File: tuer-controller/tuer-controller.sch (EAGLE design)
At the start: 19 parts, among them IC1 ATTINY24/44/84-PU

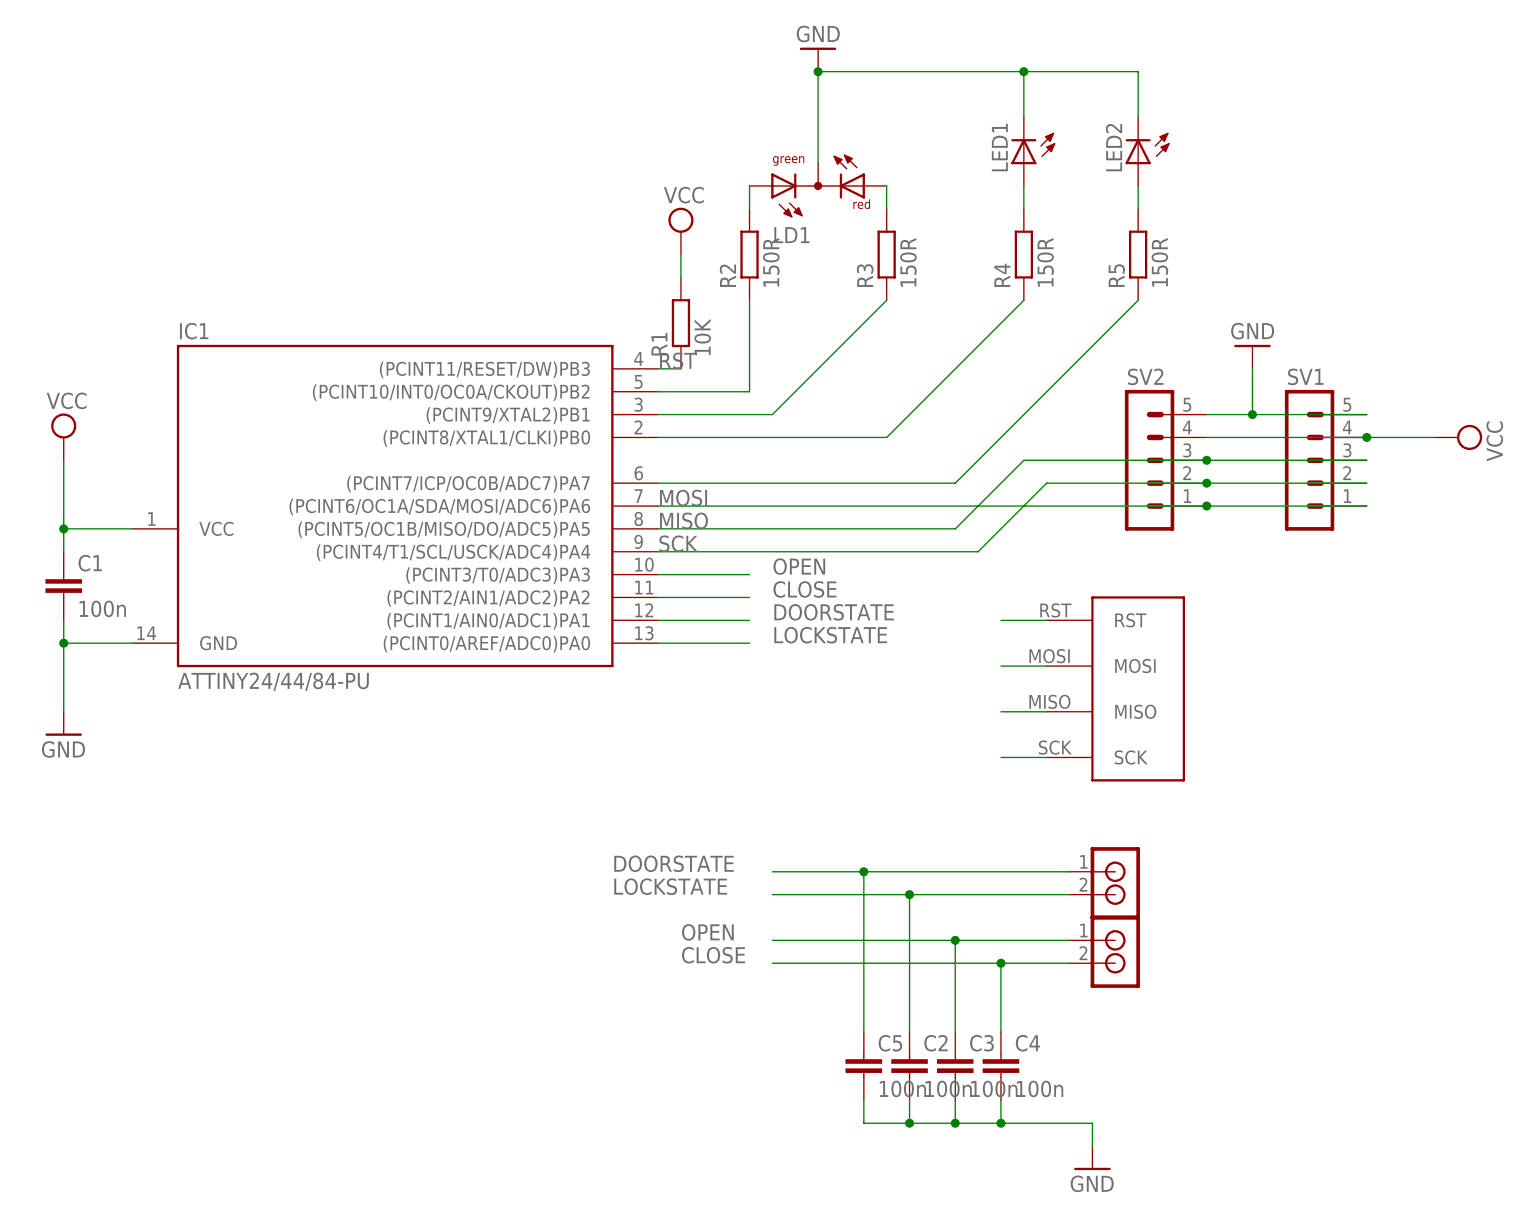
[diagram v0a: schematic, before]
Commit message: Tür-Controller: Taster für Not-Auf und Space-Pause (gemäß Workshop zur Schließanlage)
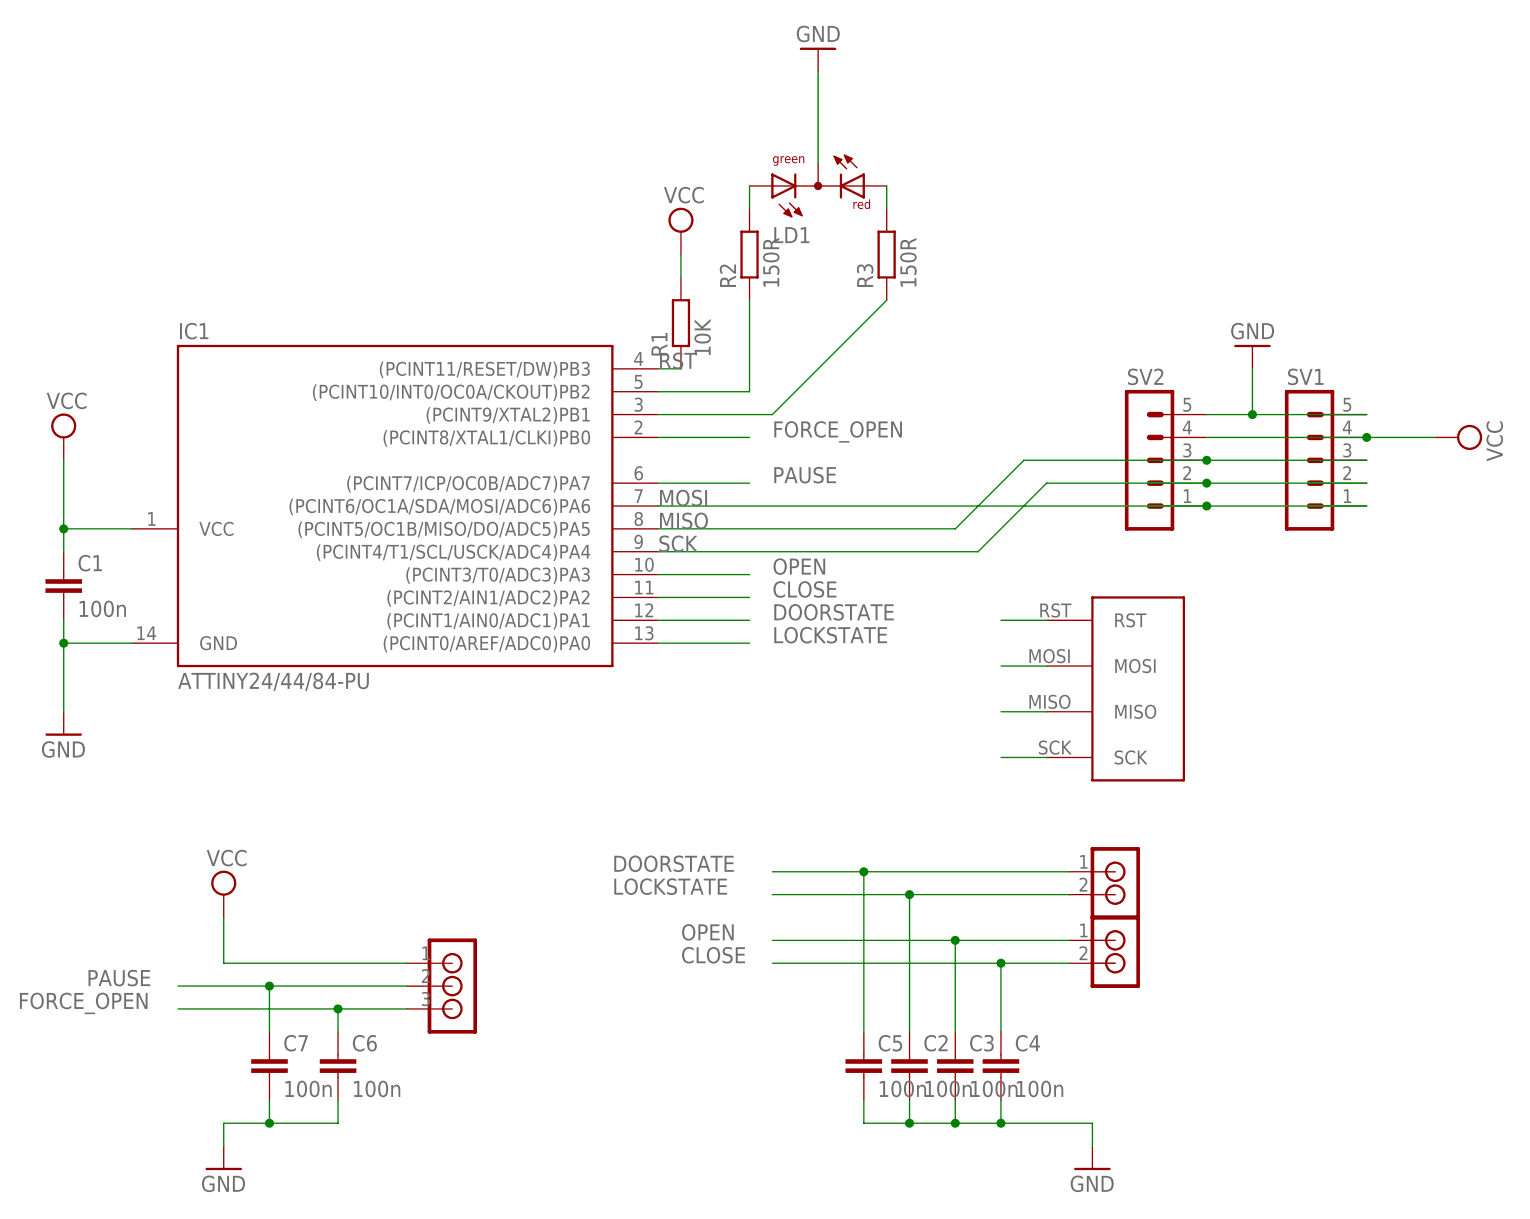
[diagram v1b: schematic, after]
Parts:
- removed LED1, LED2: (no value), led:LED5MM
- removed R4: 150R, resistor:R-EU_0207/15
- removed R5: 150R, resistor:R-EU_0207/7
- added C6, C7: 100n, resistor:C-EU025-024X044
- added U$5: RIACON_59_3, n39:RIACON_59_3
- R1: device resistor:R-EU_0207/7 -> resistor:R-EU_0207/5V
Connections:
- removed net N$10: LED2.A, R5.2
- removed net N$11: IC1.(PCINT8/XTAL1/CLKI)PB0, R4.1
- removed net N$12: IC1.(PCINT7/ICP/OC0B/ADC7)PA7, R5.1
- removed net N$9: LED1.A, R4.2
- new net FORCE_OPEN: C6.1, IC1.(PCINT8/XTAL1/CLKI)PB0, U$5.3
- new net PAUSE: C7.1, IC1.(PCINT7/ICP/OC0B/ADC7)PA7, U$5.2
- net GND: now also C6.2, C7.2; no longer LED1.C, LED2.C
- net VCC: now also U$5.1
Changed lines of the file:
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@@
 <parts>
 <part name="SUPPLY1" library="supply2" deviceset="VCC" device=""/>
-<part name="R1" library="resistor" deviceset="R-EU_" device="0207/7" value="10K"/>
+<part name="R1" library="resistor" deviceset="R-EU_" device="0207/5V" value="10K"/>
 <part name="C1" library="resistor" deviceset="C-EU" device="025-024X044" value="100n"/>
 <part name="SV2" library="con-lstb" deviceset="MA05-1" device=""/>
@@
 <part name="C5" library="resistor" deviceset="C-EU" device="025-024X044" value="100n"/>
 <part name="GND3" library="supply1" deviceset="GND" device=""/>
-<part name="LED1" library="led" deviceset="LED" device="5MM"/>
-<part name="LED2" library="led" deviceset="LED" device="5MM"/>
-<part name="R4" library="resistor" deviceset="R-EU_" device="0207/15" value="150R"/>
-<part name="R5" library="resistor" deviceset="R-EU_" device="0207/7" value="150R"/>
 <part name="SV1" library="con-lstb" deviceset="MA05-1" device=""/>
+<part name="GND5" library="supply1" deviceset="GND" device=""/>
+<part name="C6" library="resistor" deviceset="C-EU" device="025-024X044" value="100n"/>
+<part name="SUPPLY2" library="supply2" deviceset="VCC" device=""/>
+<part name="C7" library="resistor" deviceset="C-EU" device="025-024X044" value="100n"/>
+<part name="U$5" library="n39" deviceset="RIACON_59_3" device=""/>
 </parts>
 <sheets>
@@
 <instance part="C5" gate="G$1" x="40.64" y="-2.54"/>
 <instance part="GND3" gate="1" x="66.04" y="-15.24"/>
-<instance part="LED1" gate="G$1" x="58.42" y="96.52" rot="R180"/>
-<instance part="LED2" gate="G$1" x="71.12" y="96.52" rot="R180"/>
-<instance part="R4" gate="G$1" x="58.42" y="86.36" rot="R90"/>
-<instance part="R5" gate="G$1" x="71.12" y="86.36" rot="R90"/>
 <instance part="SV1" gate="G$1" x="88.9" y="63.5"/>
+<instance part="GND5" gate="1" x="-30.48" y="-15.24"/>
+<instance part="C6" gate="G$1" x="-17.78" y="-2.54"/>
+<instance part="SUPPLY2" gate="G$1" x="-30.48" y="15.24"/>
+<instance part="C7" gate="G$1" x="-25.4" y="-2.54"/>
+<instance part="U$5" gate="G$1" x="-5.08" y="5.08"/>
 </instances>
 <busses>
@@
 <junction x="96.52" y="66.04"/>
 </segment>
+<segment>
+<pinref part="SUPPLY2" gate="G$1" pin="VCC"/>
+<wire x1="-30.48" y1="12.7" x2="-30.48" y2="7.62" width="0.1524" layer="91"/>
+<pinref part="U$5" gate="G$1" pin="1"/>
+<wire x1="-30.48" y1="7.62" x2="-10.16" y2="7.62" width="0.1524" layer="91"/>
+</segment>
 </net>
 <net name="GND" class="0">
@@
 <pinref part="GND2" gate="1" pin="GND"/>
 <wire x1="35.56" y1="96.52" x2="35.56" y2="106.68" width="0.1524" layer="91"/>
-<pinref part="LED2" gate="G$1" pin="C"/>
-<wire x1="71.12" y1="101.6" x2="71.12" y2="106.68" width="0.1524" layer="91"/>
-<wire x1="71.12" y1="106.68" x2="58.42" y2="106.68" width="0.1524" layer="91"/>
-<junction x="35.56" y="106.68"/>
-<pinref part="LED1" gate="G$1" pin="C"/>
-<wire x1="58.42" y1="106.68" x2="35.56" y2="106.68" width="0.1524" layer="91"/>
-<wire x1="58.42" y1="101.6" x2="58.42" y2="106.68" width="0.1524" layer="91"/>
-<junction x="58.42" y="106.68"/>
 </segment>
 <segment>
@@
 <junction x="55.88" y="-10.16"/>
 </segment>
+<segment>
+<pinref part="C6" gate="G$1" pin="2"/>
+<wire x1="-17.78" y1="-7.62" x2="-17.78" y2="-10.16" width="0.1524" layer="91"/>
+<pinref part="GND5" gate="1" pin="GND"/>
+<wire x1="-17.78" y1="-10.16" x2="-25.4" y2="-10.16" width="0.1524" layer="91"/>
+<wire x1="-25.4" y1="-10.16" x2="-30.48" y2="-10.16" width="0.1524" layer="91"/>
+<wire x1="-30.48" y1="-10.16" x2="-30.48" y2="-12.7" width="0.1524" layer="91"/>
+<pinref part="C7" gate="G$1" pin="2"/>
+<wire x1="-25.4" y1="-7.62" x2="-25.4" y2="-10.16" width="0.1524" layer="91"/>
+<junction x="-25.4" y="-10.16"/>
+</segment>
 </net>
 <net name="MISO" class="0">
@@
 </segment>
 </net>
-<net name="N$9" class="0">
-<segment>
-<pinref part="R4" gate="G$1" pin="2"/>
-<pinref part="LED1" gate="G$1" pin="A"/>
-<wire x1="58.42" y1="91.44" x2="58.42" y2="93.98" width="0.1524" layer="91"/>
-</segment>
-</net>
-<net name="N$10" class="0">
-<segment>
-<pinref part="R5" gate="G$1" pin="2"/>
-<pinref part="LED2" gate="G$1" pin="A"/>
-<wire x1="71.12" y1="91.44" x2="71.12" y2="93.98" width="0.1524" layer="91"/>
-</segment>
-</net>
-<net name="N$11" class="0">
-<segment>
-<pinref part="IC1" gate="1" pin="(PCINT8/XTAL1/CLKI)PB0"/>
-<wire x1="17.78" y1="66.04" x2="43.18" y2="66.04" width="0.1524" layer="91"/>
-<pinref part="R4" gate="G$1" pin="1"/>
-<wire x1="43.18" y1="66.04" x2="58.42" y2="81.28" width="0.1524" layer="91"/>
-</segment>
-</net>
-<net name="N$12" class="0">
-<segment>
-<pinref part="IC1" gate="1" pin="(PCINT7/ICP/OC0B/ADC7)PA7"/>
-<wire x1="17.78" y1="60.96" x2="50.8" y2="60.96" width="0.1524" layer="91"/>
-<pinref part="R5" gate="G$1" pin="1"/>
-<wire x1="50.8" y1="60.96" x2="71.12" y2="81.28" width="0.1524" layer="91"/>
-</segment>
-</net>
 <net name="DOORSTATE" class="0">
 <segment>
@@
 </segment>
 </net>
+<net name="FORCE_OPEN" class="0">
+<segment>
+<pinref part="IC1" gate="1" pin="(PCINT8/XTAL1/CLKI)PB0"/>
+<wire x1="17.78" y1="66.04" x2="27.94" y2="66.04" width="0.1524" layer="91"/>
+<label x="30.48" y="66.04" size="1.778" layer="95"/>
+</segment>
+<segment>
+<wire x1="-10.16" y1="2.54" x2="-17.78" y2="2.54" width="0.1524" layer="91"/>
+<pinref part="C6" gate="G$1" pin="1"/>
+<wire x1="-17.78" y1="0" x2="-17.78" y2="2.54" width="0.1524" layer="91"/>
+<junction x="-17.78" y="2.54"/>
+<wire x1="-17.78" y1="2.54" x2="-35.56" y2="2.54" width="0.1524" layer="91"/>
+<label x="-53.34" y="2.54" size="1.778" layer="95"/>
+<pinref part="U$5" gate="G$1" pin="3"/>
+</segment>
+</net>
+<net name="PAUSE" class="0">
+<segment>
+<pinref part="IC1" gate="1" pin="(PCINT7/ICP/OC0B/ADC7)PA7"/>
+<wire x1="17.78" y1="60.96" x2="27.94" y2="60.96" width="0.1524" layer="91"/>
+<label x="30.48" y="60.96" size="1.778" layer="95"/>
+</segment>
+<segment>
+<wire x1="-10.16" y1="5.08" x2="-25.4" y2="5.08" width="0.1524" layer="91"/>
+<pinref part="C7" gate="G$1" pin="1"/>
+<wire x1="-25.4" y1="0" x2="-25.4" y2="5.08" width="0.1524" layer="91"/>
+<junction x="-25.4" y="5.08"/>
+<wire x1="-25.4" y1="5.08" x2="-35.56" y2="5.08" width="0.1524" layer="91"/>
+<label x="-45.72" y="5.08" size="1.778" layer="95"/>
+<pinref part="U$5" gate="G$1" pin="2"/>
+</segment>
+</net>
